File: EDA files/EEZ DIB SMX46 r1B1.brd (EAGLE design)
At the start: 146 x 95 mm, 157 parts, among them IC1 STM32F030C6T6, IC2 74HC1G126GW,125, IC3 M24C32-WMN6P, IC4 LP2985-33DBVR, IC5 74HC2G04GW,125, IC6 OPA2170, K1 FTR-C1GA012G-B05, K10 FTR-C1GA012G-B05, K11 FTR-C1GA012G-B05, K12 FTR-C1GA012G-B05, K13 FTR-C1GA012G-B05, K14 FTR-C1GA012G-B05, K15 FTR-C1GA012G-B05, K16 FTR-C1GA012G-B05, K17 FTR-C1GA012G-B05, K18 FTR-C1GA012G-B05, K19 FTR-C1GA012G-B05, K2 FTR-C1GA012G-B05, K20 FTR-C1GA012G-B05, K21 FTR-C1GA012G-B05, K22 FTR-C1GA012G-B05, K23 FTR-C1GA012G-B05, K24 FTR-C1GA012G-B05, K3 FTR-C1GA012G-B05, K4 FTR-C1GA012G-B05, K5 FTR-C1GA012G-B05, K6 FTR-C1GA012G-B05, K7 FTR-C1GA012G-B05, K8 FTR-C1GA012G-B05, K9 FTR-C1GA012G-B05, Q1 2N7002, Q10 2N7002, Q11 2N7002, Q12 2N7002, Q13 2N7002, Q14 2N7002, Q15 2N7002, Q16 2N7002, Q17 2N7002, Q18 2N7002, Q19 2N7002, Q2 2N7002, Q20 2N7002, Q21 2N7002, Q22 2N7002, Q23 2N7002, Q24 2N7002, Q25 2N7002, Q3 2N7002, Q4 2N7002, Q5 2N7002, Q6 2N7002, Q7 2N7002, Q8 2N7002, Q9 2N7002, X1 SSW-106-02-S-S, X2 77317-104-28LF, X3 691327310016, X4 691327310016

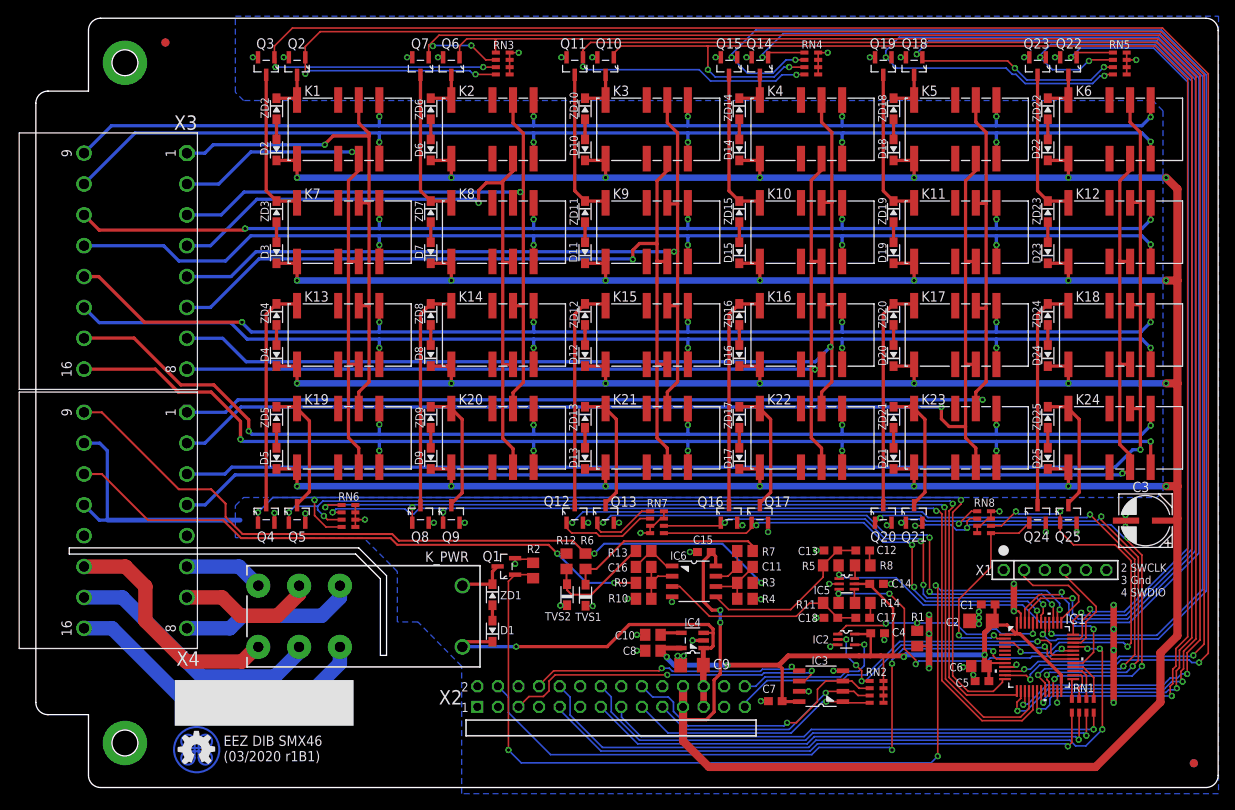
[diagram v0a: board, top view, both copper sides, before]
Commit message: front panel connectors position adjusted
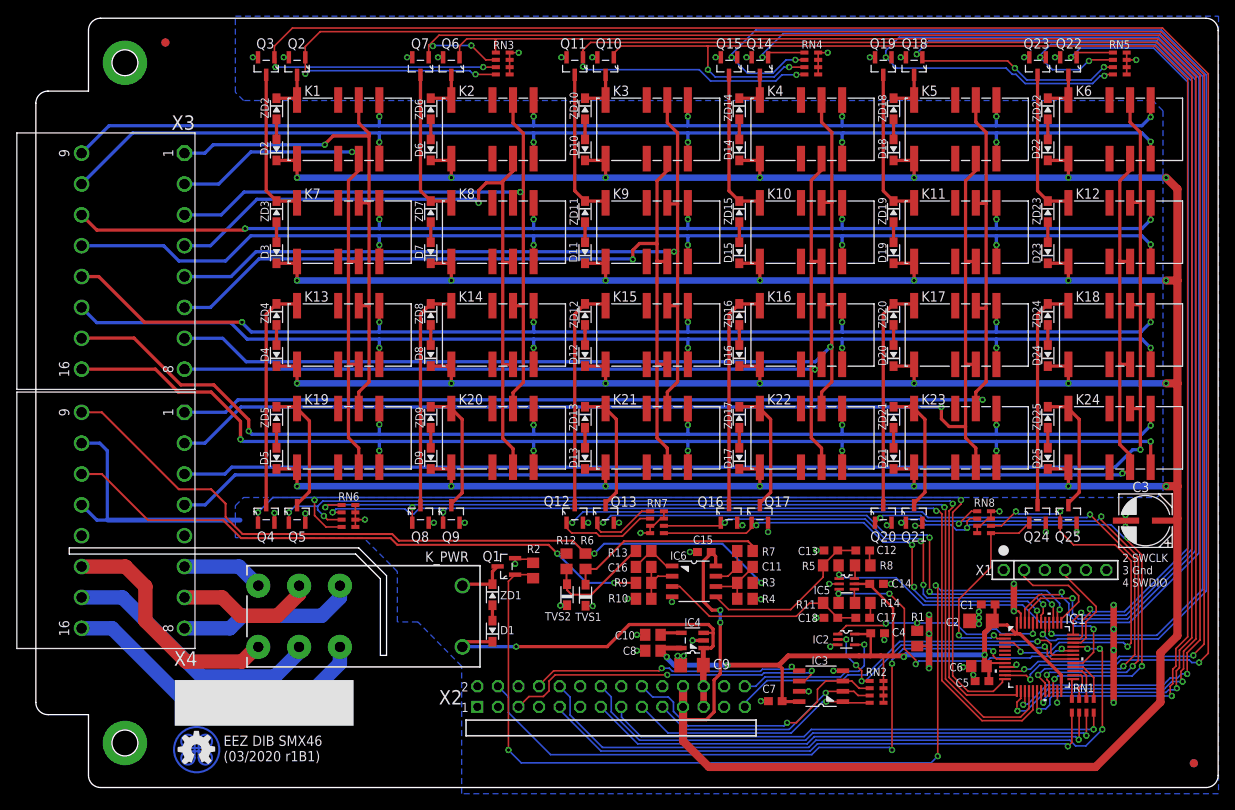
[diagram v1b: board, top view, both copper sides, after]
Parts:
- moved X3 0.30 mm to (12.0, 65.0)
- moved X4 0.30 mm to (12.0, 33.0)
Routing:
- net GND: track 132.7 -> 133.3 mm
